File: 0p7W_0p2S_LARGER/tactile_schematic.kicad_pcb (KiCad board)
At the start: 2 copper layers, 145.2 x 85.6 mm, 55 parts, among them IC1 CY8C4145PVI-PS431, J1 Conn_01x03, J2 Conn_01x04, J3 Conn_01x04, J4 Conn_01x03, J5 Conn_ARM_SWD_TagConnect_TC203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

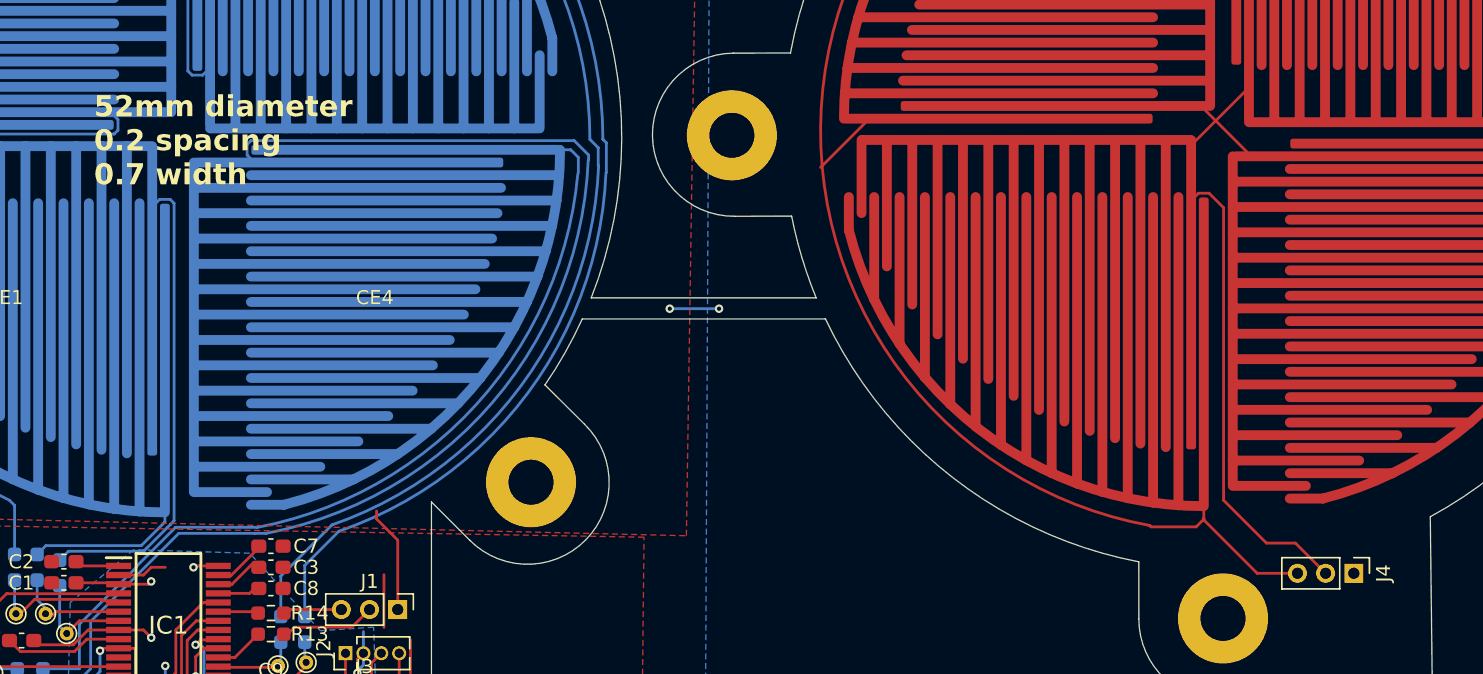
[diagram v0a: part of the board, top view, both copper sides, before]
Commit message: fixed silkscreen
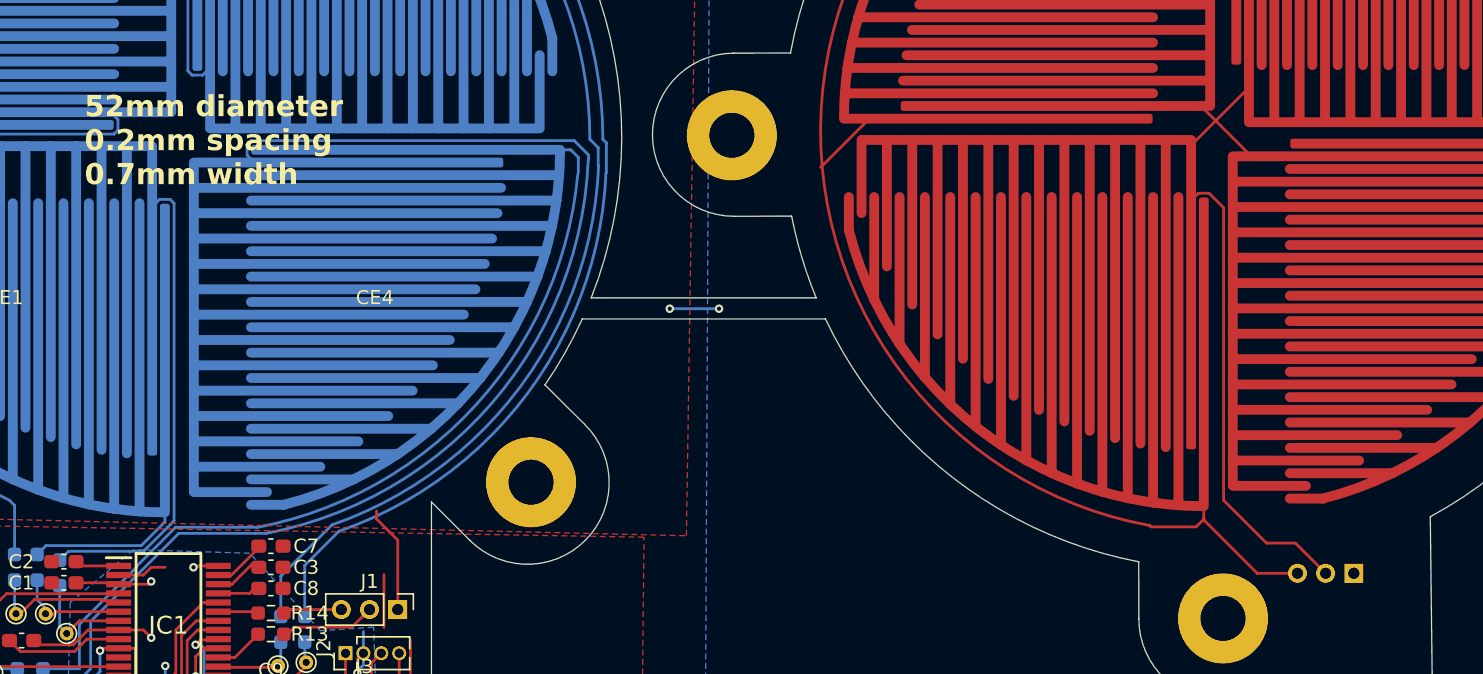
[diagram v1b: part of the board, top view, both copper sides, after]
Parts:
- J4: moved to B.Cu
- turned J4 to 90 degrees
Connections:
- net SHEILD renamed SHIELD
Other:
- board text added: "52mm diameter 0.2mm spacing 0.7mm width"
- board text removed: "52mm diameter 0.2 spacing 0.7 width"

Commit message: more spacing fixes
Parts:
- moved J4 3.45 mm to (196.8, 112.4)
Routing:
- net Net-(J1-Pin_3): track 73.3 -> 70.4 mm
- net SHIELD: track 26.8 -> 24.4 mm
- net Net-(J1-Pin_2): track 96.8 -> 95.7 mm
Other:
- outline, holes or cut-outs redrawn
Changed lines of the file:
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@@
 			(psa4output no)
 			(plot_black_and_white yes)
-			(plotinvisibletext no)
 			(sketchpadsonfab no)
 			(plotpadnumbers no)
@@
 	(footprint "Connector_PinHeader_2.00mm:PinHeader_1x03_P2.00mm_Vertical"
 		(layer "B.Cu")
-		(at 198.455208 115.421992 90)
+		(at 196.8 112.4 90)
 		(descr "Through hole straight pin header, 1x03, 2.00mm pitch, single row")
 		(tags "Through hole pin header THT 1x03 2.00mm single row")
@@
 	(gr_arc
 		(start 219.613758 89.883864)
-		(mid 214.17166 102.414952)
-		(end 203.884742 111.405164)
+		(mid 211.022144 106.088748)
+		(end 194.79456 114.63741)
 		(stroke
 			(width 0.076)
@@
 	)
 	(gr_line
-		(start 204.022001 123.020583)
-		(end 203.884742 111.405164)
-		(stroke
-			(width 0.076)
-			(type default)
-		)
-		(layer "Edge.Cuts")
-	)
-	(gr_line
 		(start 135.756738 55.919088)
 		(end 132.916505 58.776131)
@@
 	)
 	(gr_line
-		(start 192.807244 123.020583)
-		(end 204.022001 123.020583)
+		(start 194.8 118.7)
+		(end 194.79456 114.63741)
 		(stroke
 			(width 0.076)
@@
 	)
 	(gr_arc
-		(start 192.807244 123.020583)
-		(mid 186.596346 123.946133)
+		(start 194.8 118.7)
+		(mid 188.980924 124.473576)
 		(end 183.193351 118.668423)
 		(stroke
@@
 	)
 	(segment
-		(start 122.988103 117.996125)
-		(end 122.488103 118.496125)
+		(start 188.037239 111.862761)
+		(end 189.562761 111.862761)
 		(width 0.2)
 		(layer "F.Cu")
@@
 	)
 	(segment
-		(start 194.455208 115.421992)
-		(end 191.59647 115.421992)
+		(start 122.988103 117.996125)
+		(end 122.488103 118.496125)
 		(width 0.2)
 		(layer "F.Cu")
@@
 	)
 	(segment
+		(start 192.7 112.3)
+		(end 192.8 112.4)
+		(width 0.2)
+		(layer "F.Cu")
+		(net 21)
+	)
+	(segment
 		(start 187.805603 99.714125)
 		(end 187.805603 111.516125)
@@
 	)
 	(segment
+		(start 189.562761 111.862761)
+		(end 190 112.3)
+		(width 0.2)
+		(layer "F.Cu")
+		(net 21)
+	)
+	(segment
 		(start 187.805603 111.516125)
 		(end 187.805603 111.580212)
@@
 	)
 	(segment
+		(start 190 112.3)
+		(end 192.7 112.3)
+		(width 0.2)
+		(layer "F.Cu")
+		(net 21)
+	)
+	(segment
 		(start 184.059436 112.126125)
 		(end 183.958912 112.025601)
@@
 	)
 	(segment
+		(start 187.805603 111.516125)
+		(end 187.805603 111.631125)
+		(width 0.2)
+		(layer "F.Cu")
+		(net 21)
+	)
+	(segment
 		(start 164.063113 83.145125)
 		(end 160.598273 86.609965)
@@
 	(segment
 		(start 187.805603 111.631125)
-		(end 187.805603 111.516125)
+		(end 188.037239 111.862761)
 		(width 0.2)
 		(layer "F.Cu")
@@
 	)
 	(segment
-		(start 191.59647 115.421992)
-		(end 187.805603 111.631125)
-		(width 0.2)
-		(layer "F.Cu")
-		(net 21)
-	)
-	(segment
 		(start 217.4 82.03)
 		(end 217.4 81.43)
@@
 	)
 	(segment
-		(start 110.761108 120.746125)
-		(end 111.848608 120.746125)
-		(width 0.2)
-		(layer "F.Cu")
-		(net 41)
-	)
-	(segment
 		(start 109.614261 120.746125)
 		(end 109.442452 120.917934)
@@
 	)
 	(segment
-		(start 111.848608 120.746125)
-		(end 111.949608 120.847125)
-		(width 0.2)
-		(layer "F.Cu")
-		(net 41)
-	)
-	(segment
-		(start 111.848608 123.346125)
-		(end 110.761108 123.346125)
-		(width 0.2)
-		(layer "F.Cu")
-		(net 41)
-	)
-	(segment
-		(start 111.949608 123.245125)
-		(end 111.848608 123.346125)
-		(width 0.2)
-		(layer "F.Cu")
-		(net 41)
-	)
-	(segment
-		(start 111.949608 120.847125)
-		(end 111.949608 123.245125)
+		(start 115.432629 113.186125)
+		(end 115.432629 111.632629)
 		(width 0.2)
 		(layer "F.Cu")
@@
 	)
 	(via
-		(at 153.390603 96.636125)
+		(at 150.75 96.636125)
 		(size 0.6)
 		(drill 0.3)
@@
 	)
 	(via
-		(at 150.400603 69.956125)
+		(at 149.35 69.85)
 		(size 0.6)
 		(drill 0.3)
@@
 	)
 	(via
-		(at 149.890603 96.636125)
+		(at 149.1 96.65)
 		(size 0.6)
 		(drill 0.3)
@@
 	)
 	(via
-		(at 106.265603 125.576125)
+		(at 115.432629 113.186125)
 		(size 0.6)
 		(drill 0.3)
@@
 	)
 	(via
-		(at 153.900603 69.956125)
+		(at 151.05 69.956125)
 		(size 0.6)
 		(drill 0.3)
@@
 	)
 	(segment
-		(start 109.442452 122.399276)
+		(start 149.456125 69.956125)
+		(end 149.35 69.85)
+		(width 0.2)
+		(layer "B.Cu")
+		(net 41)
+	)
+	(segment
+		(start 109.442452 118.741376)
 		(end 109.442452 120.917934)
 		(width 0.2)
@@
 	)
 	(segment
-		(start 150.400603 69.956125)
-		(end 153.900603 69.956125)
+		(start 114.997703 113.186125)
+		(end 109.442452 118.741376)
 		(width 0.2)
 		(layer "B.Cu")
@@
 	)
 	(segment
-		(start 106.265603 125.576125)
-		(end 109.442452 122.399276)
+		(start 115.432629 113.186125)
+		(end 114.997703 113.186125)
 		(width 0.2)
 		(layer "B.Cu")
@@
 	)
 	(segment
-		(start 153.390603 96.636125)
-		(end 149.890603 96.636125)
+		(start 151.05 69.956125)
+		(end 149.456125 69.956125)
 		(width 0.2)
 		(layer "B.Cu")
@@
 	)
 	(segment
-		(start 194.30934 113.276125)
-		(end 196.455207 115.421992)
+		(start 149.113875 96.636125)
+		(end 149.1 96.65)
+		(width 0.2)
+		(layer "B.Cu")
+		(net 41)
+	)
+	(segment
+		(start 150.75 96.636125)
+		(end 149.113875 96.636125)
+		(width 0.2)
+		(layer "B.Cu")
+		(net 41)
+	)
+	(segment
+		(start 187.428589 88.438125)
+		(end 188.182617 88.438125)
+		(width 0.2)
+		(layer "F.Cu")
+		(net 42)
+	)
+	(segment
+		(start 193.749999 111.350001)
+		(end 194.699998 112.3)
+		(width 0.2)
+		(layer "F.Cu")
+		(net 42)
+	)
+	(segment
+		(start 193.499999 111.1)
+		(end 193.749999 111.350001)
 		(width 0.2)
 		(layer "F.Cu")
@@
 	)
 	(segment
+		(start 189.209603 111.1)
+		(end 193.499999 111.1)
+		(width 0.2)
+		(layer "F.Cu")
+		(net 42)
+	)
+	(segment
+		(start 193.749999 111.350001)
+		(end 194.799999 112.4)
+		(width 0.2)
+		(layer "F.Cu")
+		(net 42)
+	)
+	(segment
 		(start 191.010603 80.932472)
 		(end 191.010603 72.395125)
@@
 	)
 	(segment
-		(start 127.325603 119.246125)
-		(end 128.575602 117.996126)
+		(start 186.905603 95.656125)
+		(end 186.905603 88.961111)
 		(width 0.2)
 		(layer "F.Cu")
@@
 	)
 	(segment
-		(start 186.905603 88.961111)
-		(end 187.428589 88.438125)
+		(start 127.325603 119.246125)
+		(end 128.575602 117.996126)
 		(width 0.2)
 		(layer "F.Cu")
@@
 	)
 	(segment
-		(start 187.428589 88.438125)
-		(end 188.182617 88.438125)
-		(width 0.2)
-		(layer "F.Cu")
-		(net 42)
-	)
-	(segment
 		(start 177.255603 82.245125)
 		(end 187.604603 82.245125)
@@
 	)
 	(segment
-		(start 186.905603 95.656125)
-		(end 186.905603 88.961111)
+		(start 189.209603 89.465111)
+		(end 189.209603 111.1)
 		(width 0.2)
 		(layer "F.Cu")
@@
 	)
 	(segment
-		(start 189.209603 110.235125)
-		(end 192.250603 113.276125)
-		(width 0.2)
-		(layer "F.Cu")
-		(net 42)
-	)
-	(segment
 		(start 191.175603 85.816125)
 		(end 200.860603 85.816125)
@@
 	)
 	(segment
-		(start 189.209603 89.465111)
-		(end 189.209603 110.235125)
-		(width 0.2)
-		(layer "F.Cu")
-		(net 42)
-	)
-	(segment
-		(start 192.250603 113.276125)
-		(end 194.30934 113.276125)
+		(start 186.905603 88.961111)
+		(end 187.428589 88.438125)
 		(width 0.2)
 		(layer "F.Cu")
@@
 		(hatch edge 0.5)
 		(connect_pads
-			(clearance 0.5)
+			(clearance 0.35)
 		)
-		(min_thickness 0.25)
+		(min_thickness 0.2)
 		(filled_areas_thickness no)
 		(fill yes
-			(thermal_gap 0.5)
+			(thermal_gap 0.4)
 			(thermal_bridge_width 0.5)
 		)
@@
 		(polygon
 			(pts
-				(xy 152.850603 40.686125) (xy 152.420603 126.336125) (xy 232.400603 126.586125) (xy 231.110603 40.686125)
+				(xy 148.967067 40.686125) (xy 148.537128 126.323986) (xy 232.400603 126.586125) (xy 231.110603 40.686125)
 			)
 		)
